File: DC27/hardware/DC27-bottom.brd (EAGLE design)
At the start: 102.8 x 200.9 mm, 86 parts, among them IC2 LDL112D33R, IC3 FT2232HL-REEL, IC4 93LC46BT-I_OT, J1 DN PAIR, J2 JTAG, J3 Battery, U2 ESP-WROOM-32, Y1 ABM7-12.000MHZ-D2Y-T

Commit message: nearly done
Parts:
- moved U$9 95.7 mm to (53.5, 104.8)
- moved U$8 59.2 mm to (89.3, 14.9)
- moved U$7 34.1 mm to (12.2, 14.6)
- moved J1 29.6 mm to (24.0, 103.9), turned to 0 degrees
- moved J2 16.7 mm to (78.5, 71.6), turned to 0 degrees
- moved R6 14.9 mm to (50.9, 36.7)
- moved EMIFILTER1 10.4 mm to (48.2, 37.4)
- moved R15 9.43 mm to (7.30, 52.3), turned to 0 degrees
- moved R18 9.17 mm to (8.18, 41.7), turned to 90 degrees
- moved R4 9.06 mm to (6.78, 92.0)
- moved R11 8.86 mm to (36.8, 72.3), turned to 90 degrees
- moved EMIFILTER2 8.81 mm to (55.0, 40.7), turned to 180 degrees
- moved R24 8.72 mm to (77.3, 76.0)
- moved C34 8.31 mm to (7.80, 45.4), turned to 90 degrees
- moved R12 8.01 mm to (34.5, 72.3), turned to 90 degrees
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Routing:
- net VCC: track 0.00 -> 616.0 mm, vias 0 -> 11
- net DISPLAY_SD_MOSI: track 0.00 -> 207.3 mm
- net DISPLAY_SD_MISO: track 0.00 -> 161.7 mm
- net DISPLAY_SD_SCK: track 0.00 -> 156.4 mm
- net VBAT: track 0.00 -> 120.9 mm, vias 0 -> 5
- net TOUCH_IRQ: track 0.00 -> 89.0 mm, vias 0 -> 2
- net TOUCH_DATA_OUT: track 0.00 -> 86.5 mm, vias 0 -> 2
- net TOUCH_DATA_IN: track 0.00 -> 85.6 mm, vias 0 -> 2
- net SCL: track 0.00 -> 82.3 mm, vias 0 -> 1
- net DISPLAY_DATA_CMD: track 0.00 -> 80.9 mm, vias 0 -> 1
- net TOUCH_CS: track 0.00 -> 78.5 mm, vias 0 -> 2
- net SAO-GPIO2: track 0.00 -> 76.2 mm
- net TOUCH_CLK: track 0.00 -> 75.9 mm, vias 0 -> 2
- net DISPLAY_CS: track 0.00 -> 75.7 mm, vias 0 -> 1
- net SD_CS: track 0.00 -> 66.2 mm
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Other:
- board size 102.8 x 200.9 mm -> 102.4 x 117.6 mm

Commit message: what should be sent to pcbway
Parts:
- U$7: value KRUX_LOGO -> KRUX_LOGOKRUX_LOGO_SILK; device logos:KRUX_LOGO -> logos:KRUX_LOGO_SILK
- U$9: value DN_LOGODC26 -> DN_LOGO; device logos:DN_LOGO_DC26 -> logos:DN_LOGO_LONG_SILK
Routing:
- net VCC5V: track 42.9 -> 42.1 mm
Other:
- outline, holes or cut-outs redrawn
- board text added: "0 %"
- board text added: "100 %"
- board text added: "CLK"
- board text added: "GND"
- board text added: "GPIO1"
- board text added: "GPIO2"
- board text added: "Jumper all 4 for jtag via usb"
- board text added: "Jumper to use usb to program"
- board text added: "NC"
- board text added: "PWREN"
- board text added: "Pair_RX"
- board text added: "Pair_TX"
- board text added: "Prog_RX"
- board text added: "Prog_TX"
- board text added: "RXDSPI_PROMCLK"
- board text added: "SPI_PROM_CS"
- board text added: "SPI_PROM_MISO"
- board text added: "SUSPEND"
- board text added: "TDI"
- board text added: "TDO"
- board text added: "TMS"
- board text added: "TXDSPI_PROMCLK"
- board text added: "VCC"
- board text added: "jumper right 2 pins to send GPIO1/2 to top board"

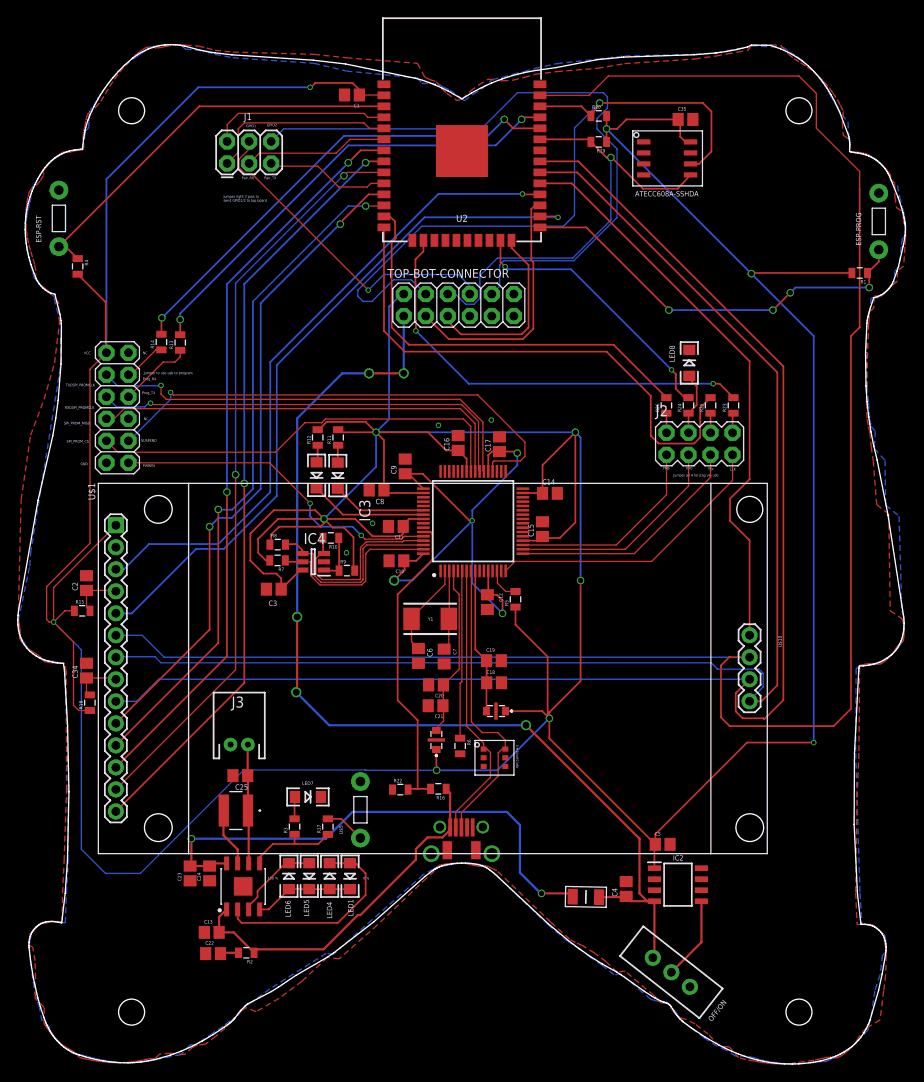
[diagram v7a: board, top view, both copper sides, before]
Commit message: Fixed artwork
Fixed artwork which got mangled by Eagle's Push and shove routing
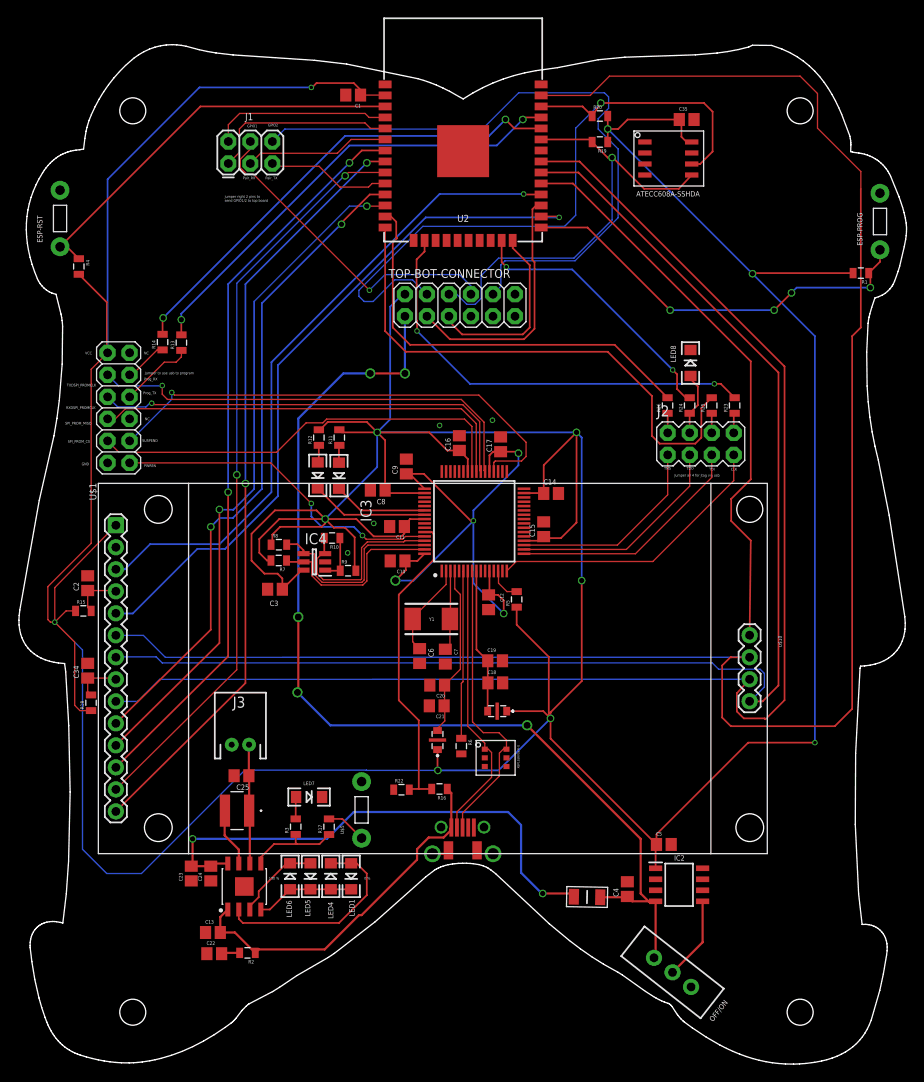
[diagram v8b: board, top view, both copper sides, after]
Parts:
- moved LED8 0.13 mm to (77.5, 80.9)
- moved R1 0.13 mm to (97.1, 91.3)
- moved R24 0.13 mm to (77.4, 76.0)
- moved R25 0.13 mm to (79.9, 76.0)
- moved OFF/ON 0.13 mm to (75.4, 10.6)
- moved RESETTABLE_FUSE 0.13 mm to (65.6, 19.3)
- moved R18 0.13 mm to (8.32, 41.7)
- moved C1 0.13 mm to (38.6, 111.8)
- moved C12 0.13 mm to (54.2, 53.3)
- moved C14 0.13 mm to (61.4, 65.8)
- moved C15 0.13 mm to (60.5, 61.7)
- moved C16 0.13 mm to (50.8, 71.6)
- moved C17 0.13 mm to (55.6, 71.5)
- moved C18 0.13 mm to (55.0, 44.0)
- moved C2 0.13 mm to (7.93, 55.5)
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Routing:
- removed copper zone on layer 1, net GND
- removed copper zone on layer 16, net GND
